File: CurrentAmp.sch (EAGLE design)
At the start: 18 parts, among them J2 CONN_4SCREW_2.54

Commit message: Minor schematic cleanup
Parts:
- removed U$1: INA212, bschulz:INA212
- added U1: INA212DCK, bschulz:INA212DCK
- J2: value CONN_4SCREW_2.54 -> CONN_42.54_SCREW; device bschulz:CONN_4SCREW_2.54 -> bschulz:CONN_42.54_SCREW
- renumbered U$2 to U2
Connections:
- net GND: now also U1.GND; no longer U$1.GND
- net N$1: now also U1.IN-; no longer U$1.IN-
- net N$2: now also U1.IN+; no longer U$1.IN+
- net REF: now also U1.REF; no longer U$1.REF
- net VCC: now also U1.V+; no longer U$1.V+
- net VOUT: now also U1.OUT; no longer U$1.OUT
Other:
- moved on the sheet: C2, C3

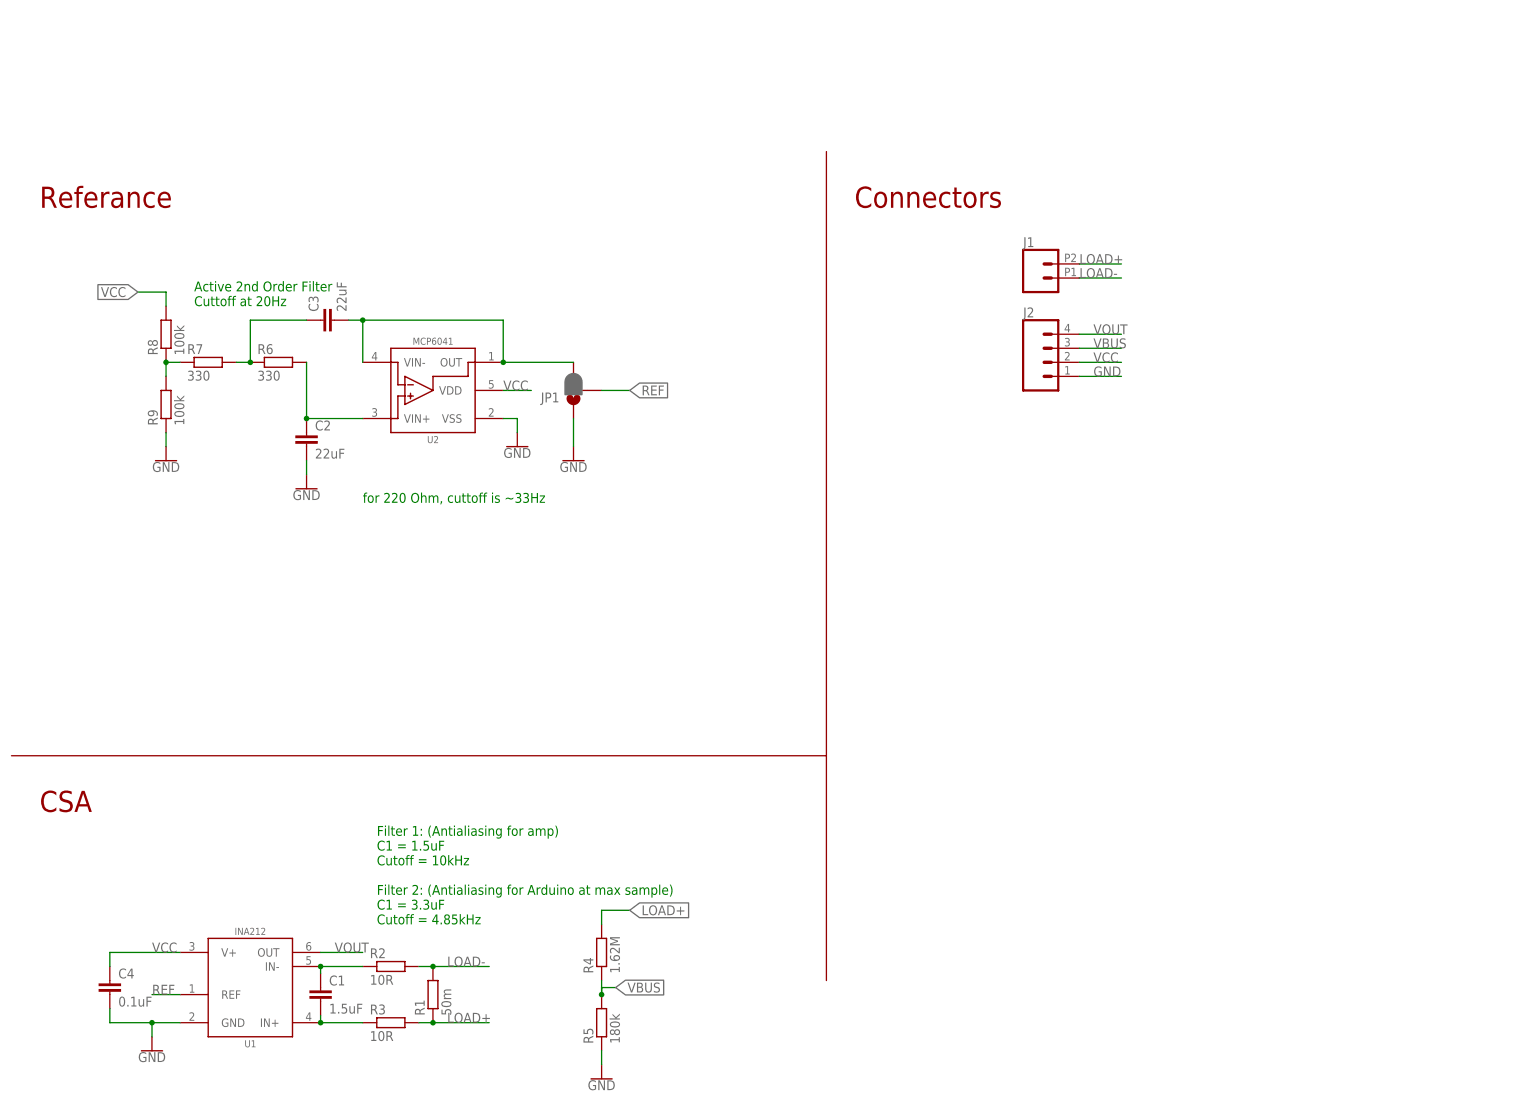
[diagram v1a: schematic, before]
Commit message: Schematic cleanup, added PDFs
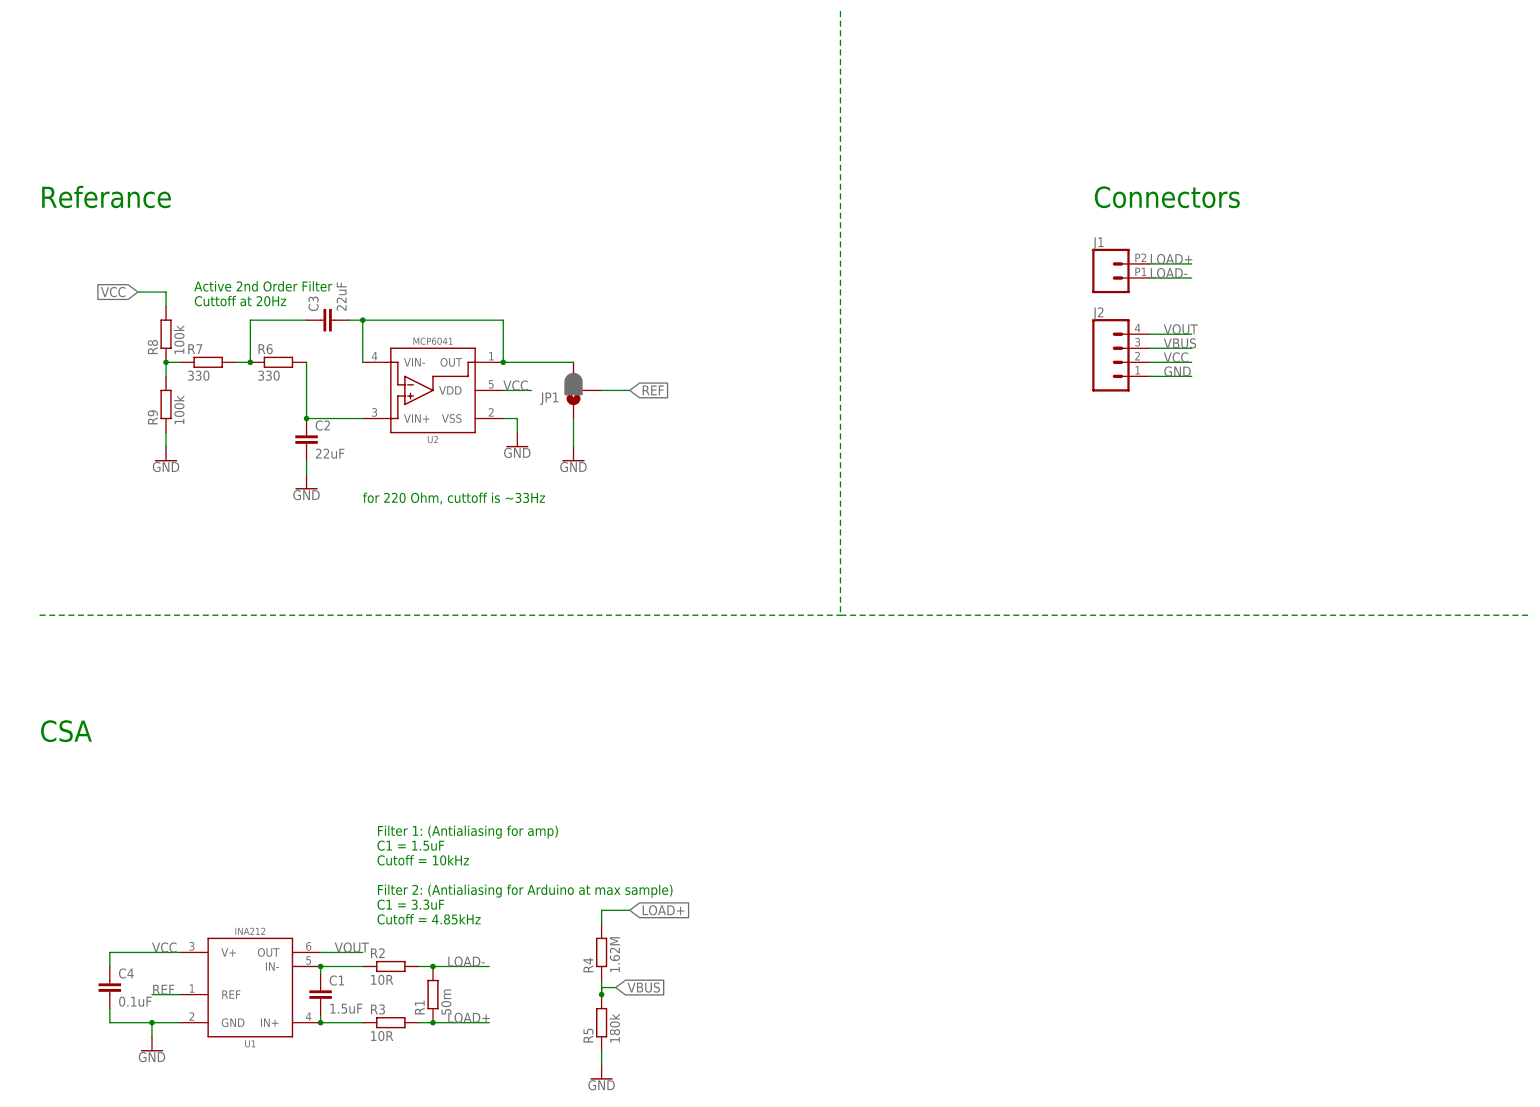
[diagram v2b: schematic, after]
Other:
- moved on the sheet: J1, J2
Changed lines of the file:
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@@
 <part name="R9" library="bschulz_passives" deviceset="R-EU_" device="R0603" value="100k"/>
 <part name="GND5" library="SparkFun-PowerSymbols" library_urn="urn:adsk.eagle:library:530" deviceset="GND" device=""/>
-<part name="FRAME3" library="frames" library_urn="urn:adsk.eagle:library:229" deviceset="LETTER_L" device=""/>
 <part name="GND6" library="SparkFun-PowerSymbols" library_urn="urn:adsk.eagle:library:530" deviceset="GND" device=""/>
 <part name="C4" library="bschulz_passives" deviceset="C-EU" device="C0603" value="0.1uF"/>
+<part name="FRAME1" library="bschulz" deviceset="FRAME_A_L" device="">
+<attribute name="DESIGNER" value="Bobby Schulz"/>
+<attribute name="PROJECT" value="Raven"/>
+<attribute name="REV" value="v0.0"/>
+</part>
 </parts>
 <sheets>
@@
 <text x="33.02" y="157.48" size="1.778" layer="91">Active 2nd Order Filter
 Cuttoff at 20Hz</text>
-<wire x1="0" y1="76.2" x2="147.32" y2="76.2" width="0.1524" layer="94"/>
-<wire x1="147.32" y1="76.2" x2="147.32" y2="35.56" width="0.1524" layer="94"/>
-<text x="5.08" y="66.04" size="3.81" layer="94" font="vector">CSA</text>
-<wire x1="147.32" y1="76.2" x2="147.32" y2="185.42" width="0.1524" layer="94"/>
-<text x="5.08" y="175.26" size="3.81" layer="94" font="vector">Referance</text>
-<text x="152.4" y="175.26" size="3.81" layer="94" font="vector">Connectors</text>
+<text x="5.08" y="78.74" size="3.81" layer="91" font="vector">CSA</text>
+<text x="5.08" y="175.26" size="3.81" layer="91" font="vector">Referance</text>
+<text x="195.58" y="175.26" size="3.81" layer="91" font="vector">Connectors</text>
 <text x="63.5" y="121.92" size="1.778" layer="91">for 220 Ohm, cuttoff is ~33Hz</text>
 </plain>
@@
 <attribute name="VALUE" x="106.68" y="17.526" size="1.778" layer="96" align="top-center"/>
 </instance>
-<instance part="FRAME3" gate="G$1" x="0" y="0" smashed="yes"/>
-<instance part="FRAME3" gate="G$2" x="147.32" y="0" smashed="yes">
-<attribute name="LAST_DATE_TIME" x="160.02" y="1.27" size="2.54" layer="94"/>
-<attribute name="SHEET" x="233.68" y="1.27" size="2.54" layer="94"/>
-<attribute name="DRAWING_NAME" x="165.1" y="19.05" size="2.54" layer="94"/>
-</instance>
 <instance part="JP1" gate="G$1" x="101.6" y="142.24" smashed="yes" rot="R180">
 <attribute name="NAME" x="99.06" y="141.859" size="1.778" layer="95" font="vector" rot="R180"/>
@@
 <attribute name="VALUE" x="27.94" y="129.286" size="1.778" layer="96" align="top-center"/>
 </instance>
-<instance part="J1" gate="G$1" x="185.42" y="162.56" smashed="yes">
-<attribute name="VALUE" x="182.88" y="157.734" size="1.778" layer="96" font="vector"/>
-<attribute name="NAME" x="182.88" y="168.148" size="1.778" layer="95" font="vector"/>
-</instance>
-<instance part="J2" gate="G$1" x="187.96" y="147.32" smashed="yes">
-<attribute name="NAME" x="182.88" y="155.448" size="1.778" layer="95" font="vector"/>
+<instance part="J1" gate="G$1" x="198.12" y="162.56" smashed="yes">
+<attribute name="VALUE" x="195.58" y="157.734" size="1.778" layer="96" font="vector"/>
+<attribute name="NAME" x="195.58" y="168.148" size="1.778" layer="95" font="vector"/>
+</instance>
+<instance part="J2" gate="G$1" x="200.66" y="147.32" smashed="yes">
+<attribute name="NAME" x="195.58" y="155.448" size="1.778" layer="95" font="vector"/>
 </instance>
 <instance part="GND6" gate="1" x="101.6" y="129.54" smashed="yes">
@@
 <attribute name="NAME" x="19.304" y="35.941" size="1.778" layer="95"/>
 <attribute name="VALUE" x="19.304" y="30.861" size="1.778" layer="96"/>
+</instance>
+<instance part="FRAME1" gate="G$1" x="0" y="0" smashed="yes">
+<attribute name="REV" x="0" y="0" size="1.778" layer="96" display="off"/>
+<attribute name="PROJECT" x="0" y="0" size="1.778" layer="96" display="off"/>
+<attribute name="DESIGNER" x="0" y="0" size="1.778" layer="96" display="off"/>
+</instance>
+<instance part="FRAME1" gate="G$2" x="172.72" y="0" smashed="yes">
+<attribute name="LAST_DATE_TIME" x="185.42" y="1.27" size="2.54" layer="94"/>
+<attribute name="SHEET" x="259.08" y="1.27" size="2.54" layer="94"/>
+<attribute name="DRAWING_NAME" x="190.5" y="19.05" size="2.54" layer="94"/>
+<attribute name="PROJECT" x="195.58" y="30.48" size="2.54" layer="94"/>
+<attribute name="DESIGNER" x="195.58" y="25.4" size="2.54" layer="94"/>
+<attribute name="REV" x="261.62" y="7.62" size="2.54" layer="94"/>
 </instance>
 </instances>
@@
 <segment>
 <pinref part="J1" gate="G$1" pin="2"/>
-<wire x1="193.04" y1="165.1" x2="200.66" y2="165.1" width="0.1524" layer="91"/>
-<label x="193.04" y="165.1" size="1.778" layer="95"/>
+<wire x1="205.74" y1="165.1" x2="213.36" y2="165.1" width="0.1524" layer="91"/>
+<label x="205.74" y="165.1" size="1.778" layer="95"/>
 </segment>
 </net>
@@
 <segment>
 <pinref part="J1" gate="G$1" pin="1"/>
-<wire x1="193.04" y1="162.56" x2="200.66" y2="162.56" width="0.1524" layer="91"/>
-<label x="193.04" y="162.56" size="1.778" layer="95"/>
+<wire x1="205.74" y1="162.56" x2="213.36" y2="162.56" width="0.1524" layer="91"/>
+<label x="205.74" y="162.56" size="1.778" layer="95"/>
 </segment>
 </net>
@@
 <segment>
 <pinref part="J2" gate="G$1" pin="1"/>
-<wire x1="193.04" y1="144.78" x2="200.66" y2="144.78" width="0.1524" layer="91"/>
-<label x="195.58" y="144.78" size="1.778" layer="95"/>
+<wire x1="205.74" y1="144.78" x2="213.36" y2="144.78" width="0.1524" layer="91"/>
+<label x="208.28" y="144.78" size="1.778" layer="95"/>
 </segment>
 <segment>
@@
 <segment>
 <pinref part="J2" gate="G$1" pin="4"/>
-<wire x1="193.04" y1="152.4" x2="200.66" y2="152.4" width="0.1524" layer="91"/>
-<label x="195.58" y="152.4" size="1.778" layer="95"/>
+<wire x1="205.74" y1="152.4" x2="213.36" y2="152.4" width="0.1524" layer="91"/>
+<label x="208.28" y="152.4" size="1.778" layer="95"/>
 </segment>
 </net>
@@
 <segment>
 <pinref part="J2" gate="G$1" pin="3"/>
-<wire x1="193.04" y1="149.86" x2="200.66" y2="149.86" width="0.1524" layer="91"/>
-<label x="195.58" y="149.86" size="1.778" layer="95"/>
+<wire x1="205.74" y1="149.86" x2="213.36" y2="149.86" width="0.1524" layer="91"/>
+<label x="208.28" y="149.86" size="1.778" layer="95"/>
 </segment>
 </net>
@@
 <segment>
 <pinref part="J2" gate="G$1" pin="2"/>
-<wire x1="193.04" y1="147.32" x2="200.66" y2="147.32" width="0.1524" layer="91"/>
-<label x="195.58" y="147.32" size="1.778" layer="95"/>
+<wire x1="205.74" y1="147.32" x2="213.36" y2="147.32" width="0.1524" layer="91"/>
+<label x="208.28" y="147.32" size="1.778" layer="95"/>
 </segment>
 </net>
@@
 </segment>
 </net>
+<net name="N$9" class="0">
+<segment>
+<wire x1="5.08" y1="101.6" x2="149.86" y2="101.6" width="0.1524" layer="91" style="longdash"/>
+<wire x1="149.86" y1="101.6" x2="274.32" y2="101.6" width="0.1524" layer="91" style="longdash"/>
+<wire x1="149.86" y1="210.82" x2="149.86" y2="101.6" width="0.1524" layer="91" style="longdash"/>
+</segment>
+</net>
